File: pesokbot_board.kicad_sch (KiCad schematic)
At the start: 0 parts

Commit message: 01_Power_Input schem
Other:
- added sheet 01_Power_Input (01_Power_Input.kicad_sch)
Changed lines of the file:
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@@
 	(generator_version "10.0")
 	(paper "A4")
+	(sheet
+		(at 87.63 71.12)
+		(size 15.24 7.62)
+		(exclude_from_sim no)
+		(in_bom yes)
+		(on_board yes)
+		(dnp no)
+		(fields_autoplaced yes)
+		(stroke
+			(width 0.1524)
+			(type solid)
+		)
+		(fill
+			(color 0 0 0 0)
+		)
+		(property "Sheetname" "01_Power_Input"
+			(at 87.63 70.4084 0)
+			(show_name no)
+			(do_not_autoplace no)
+			(effects
+				(font
+					(size 1.27 1.27)
+				)
+				(justify left bottom)
+			)
+		)
+		(property "Sheetfile" "01_Power_Input.kicad_sch"
+			(at 87.63 79.3246 0)
+			(show_name no)
+			(do_not_autoplace no)
+			(effects
+				(font
+					(size 1.27 1.27)
+				)
+				(justify left top)
+			)
+		)
+		(instances
+			(project "pesokbot_board"
+				(path "/3b0b46ed-3ce3-4874-97d9-085fc63ec69d"
+					(page "2")
+				)
+			)
+		)
+	)
 	(sheet_instances
 		(path "/"

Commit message: 02_Servo_Power in progress
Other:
- added sheet 02_Servo_Power (Servo_Power.kicad_sch)
- sheet 01_Power_Input ports: added VBAT_PROT; removed none
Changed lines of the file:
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@@
 	(generator_version "10.0")
 	(paper "A4")
+	(wire
+		(pts
+			(xy 102.87 74.93) (xy 144.78 74.93)
+		)
+		(stroke
+			(width 0)
+			(type default)
+		)
+	)
+	(sheet
+		(at 137.16 71.12)
+		(size 16.51 7.62)
+		(exclude_from_sim no)
+		(in_bom yes)
+		(on_board yes)
+		(dnp no)
+		(fields_autoplaced yes)
+		(stroke
+			(width 0.1524)
+			(type solid)
+		)
+		(fill
+			(color 0 0 0 0)
+		)
+		(property "Sheetname" "02_Servo_Power"
+			(at 137.16 70.4084 0)
+			(show_name no)
+			(do_not_autoplace no)
+			(effects
+				(font
+					(size 1.27 1.27)
+				)
+				(justify left bottom)
+			)
+		)
+		(property "Sheetfile" "Servo_Power.kicad_sch"
+			(at 137.16 79.3246 0)
+			(show_name no)
+			(do_not_autoplace no)
+			(effects
+				(font
+					(size 1.27 1.27)
+				)
+				(justify left top)
+			)
+		)
+		(instances
+			(project "pesokbot_board"
+				(path "/3b0b46ed-3ce3-4874-97d9-085fc63ec69d"
+					(page "3")
+				)
+			)
+		)
+	)
 	(sheet
 		(at 87.63 71.12)
@@
 			)
 		)
+		(pin "VBAT_PROT" input
+			(at 102.87 74.93 0)
+			(effects
+				(font
+					(size 1.27 1.27)
+				)
+				(justify right)
+			)
+		)

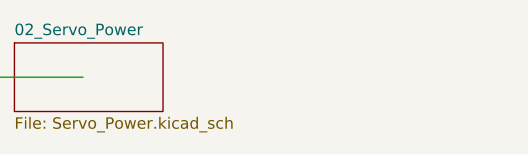
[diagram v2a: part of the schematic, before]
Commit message: BNO086 I2C connection added
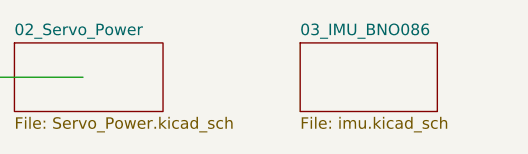
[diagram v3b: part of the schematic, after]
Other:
- added sheet 03_IMU_BNO086 (imu.kicad_sch)
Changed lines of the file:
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@@
+	)
+	(sheet
+		(at 168.91 71.12)
+		(size 15.24 7.62)
+		(exclude_from_sim no)
+		(in_bom yes)
+		(on_board yes)
+		(dnp no)
+		(fields_autoplaced yes)
+		(stroke
+			(width 0.1524)
+			(type solid)
+		)
+		(fill
+			(color 0 0 0 0)
+		)
+		(property "Sheetname" "03_IMU_BNO086"
+			(at 168.91 70.4084 0)
+			(show_name no)
+			(do_not_autoplace no)
+			(effects
+				(font
+					(size 1.27 1.27)
+				)
+				(justify left bottom)
+			)
+		)
+		(property "Sheetfile" "imu.kicad_sch"
+			(at 168.91 79.3246 0)
+			(show_name no)
+			(do_not_autoplace no)
+			(effects
+				(font
+					(size 1.27 1.27)
+				)
+				(justify left top)
+			)
+		)
+		(instances
+			(project "pesokbot_board"
+				(path "/3b0b46ed-3ce3-4874-97d9-085fc63ec69d"
+					(page "4")
+				)
+			)
+		)
 	)
 	(sheet

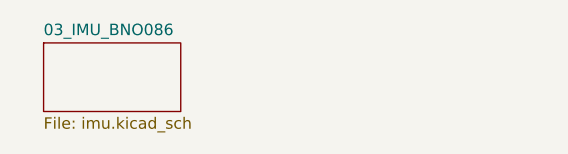
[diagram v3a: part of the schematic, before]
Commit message: add STM32H743ZIT6 schem
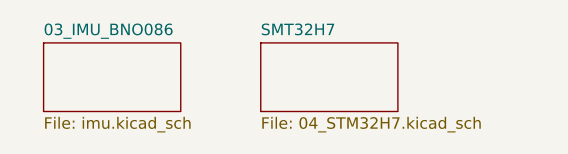
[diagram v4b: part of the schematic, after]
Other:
- added sheet SMT32H7 (04_STM32H7.kicad_sch)
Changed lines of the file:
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@@
+		)
+	)
+	(sheet
+		(at 193.04 71.12)
+		(size 15.24 7.62)
+		(exclude_from_sim no)
+		(in_bom yes)
+		(on_board yes)
+		(dnp no)
+		(fields_autoplaced yes)
+		(stroke
+			(width 0.1524)
+			(type solid)
+		)
+		(fill
+			(color 0 0 0 0)
+		)
+		(property "Sheetname" "SMT32H7"
+			(at 193.04 70.4084 0)
+			(show_name no)
+			(do_not_autoplace no)
+			(effects
+				(font
+					(size 1.27 1.27)
+				)
+				(justify left bottom)
+			)
+		)
+		(property "Sheetfile" "04_STM32H7.kicad_sch"
+			(at 193.04 79.3246 0)
+			(show_name no)
+			(do_not_autoplace no)
+			(effects
+				(font
+					(size 1.27 1.27)
+				)
+				(justify left top)
+			)
+		)
+		(instances
+			(project "pesokbot_board"
+				(path "/3b0b46ed-3ce3-4874-97d9-085fc63ec69d"
+					(page "5")
+				)
+			)
 		)
 	)

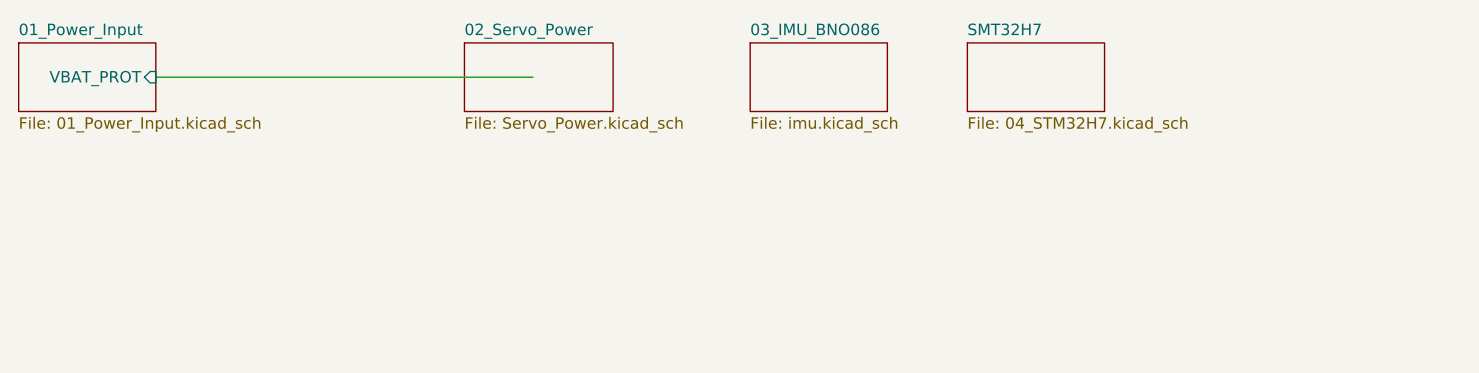
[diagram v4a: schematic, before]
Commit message: added USB-C CDC schem
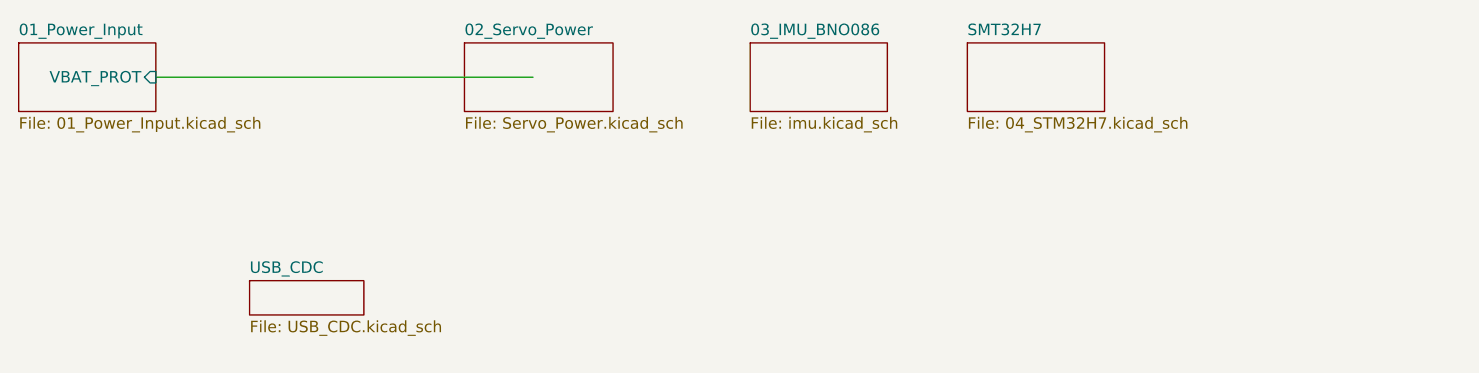
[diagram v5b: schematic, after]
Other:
- added sheet USB_CDC (USB_CDC.kicad_sch)
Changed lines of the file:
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@@
+	)
+	(sheet
+		(at 113.284 97.536)
+		(size 12.7 3.81)
+		(exclude_from_sim no)
+		(in_bom yes)
+		(on_board yes)
+		(dnp no)
+		(fields_autoplaced yes)
+		(stroke
+			(width 0.1524)
+			(type solid)
+		)
+		(fill
+			(color 0 0 0 0)
+		)
+		(property "Sheetname" "USB_CDC"
+			(at 113.284 96.8244 0)
+			(show_name no)
+			(do_not_autoplace no)
+			(effects
+				(font
+					(size 1.27 1.27)
+				)
+				(justify left bottom)
+			)
+		)
+		(property "Sheetfile" "USB_CDC.kicad_sch"
+			(at 113.284 101.9306 0)
+			(show_name no)
+			(do_not_autoplace no)
+			(effects
+				(font
+					(size 1.27 1.27)
+				)
+				(justify left top)
+			)
+		)
+		(instances
+			(project "pesokbot_board"
+				(path "/3b0b46ed-3ce3-4874-97d9-085fc63ec69d"
+					(page "6")
+				)
+			)
+		)
 	)
 	(sheet

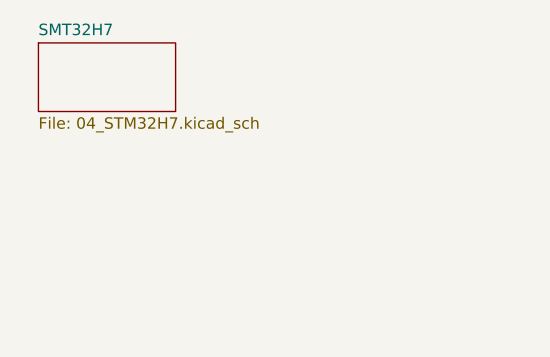
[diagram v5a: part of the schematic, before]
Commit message: added usb mcu and footprints
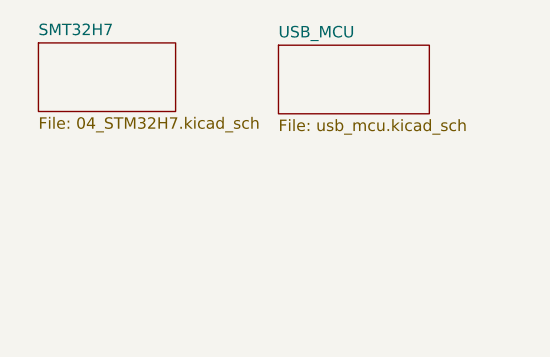
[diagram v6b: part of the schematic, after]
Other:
- added sheet USB_MCU (usb_mcu.kicad_sch)
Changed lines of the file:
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@@
+	)
+	(sheet
+		(at 219.71 71.374)
+		(size 16.764 7.62)
+		(exclude_from_sim no)
+		(in_bom yes)
+		(on_board yes)
+		(dnp no)
+		(fields_autoplaced yes)
+		(stroke
+			(width 0.1524)
+			(type solid)
+		)
+		(fill
+			(color 0 0 0 0)
+		)
+		(property "Sheetname" "USB_MCU"
+			(at 219.71 70.6624 0)
+			(show_name no)
+			(do_not_autoplace no)
+			(effects
+				(font
+					(size 1.27 1.27)
+				)
+				(justify left bottom)
+			)
+		)
+		(property "Sheetfile" "usb_mcu.kicad_sch"
+			(at 219.71 79.5786 0)
+			(show_name no)
+			(do_not_autoplace no)
+			(effects
+				(font
+					(size 1.27 1.27)
+				)
+				(justify left top)
+			)
+		)
+		(instances
+			(project "pesokbot_board"
+				(path "/3b0b46ed-3ce3-4874-97d9-085fc63ec69d"
+					(page "7")
+				)
+			)
+		)
 	)
 	(sheet

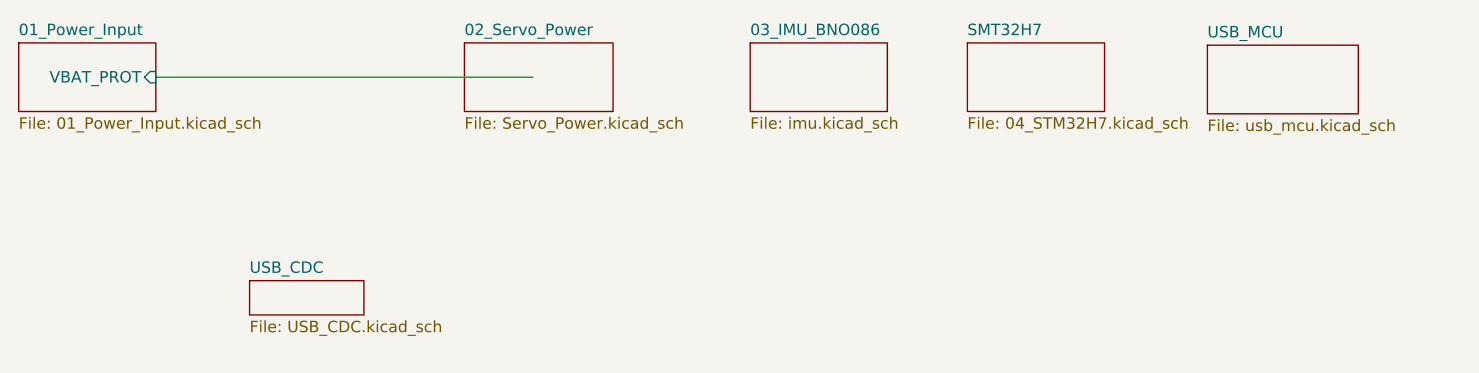
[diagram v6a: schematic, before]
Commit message: added user ports
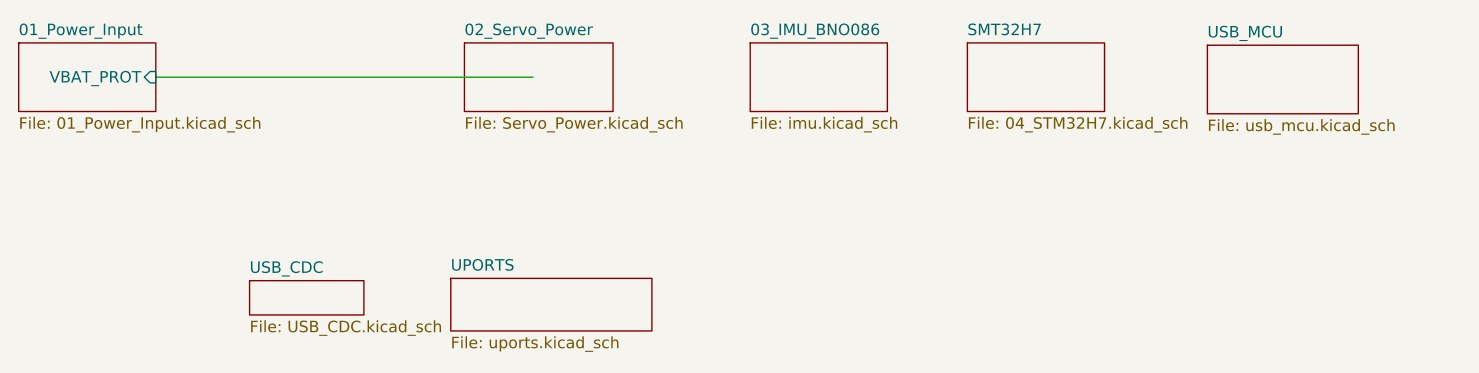
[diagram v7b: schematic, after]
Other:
- added sheet UPORTS (uports.kicad_sch)
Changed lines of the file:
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@@
+	)
+	(sheet
+		(at 135.636 97.282)
+		(size 22.352 5.842)
+		(exclude_from_sim no)
+		(in_bom yes)
+		(on_board yes)
+		(dnp no)
+		(fields_autoplaced yes)
+		(stroke
+			(width 0.1524)
+			(type solid)
+		)
+		(fill
+			(color 0 0 0 0)
+		)
+		(property "Sheetname" "UPORTS"
+			(at 135.636 96.5704 0)
+			(show_name no)
+			(do_not_autoplace no)
+			(effects
+				(font
+					(size 1.27 1.27)
+				)
+				(justify left bottom)
+			)
+		)
+		(property "Sheetfile" "uports.kicad_sch"
+			(at 135.636 103.7086 0)
+			(show_name no)
+			(do_not_autoplace no)
+			(effects
+				(font
+					(size 1.27 1.27)
+				)
+				(justify left top)
+			)
+		)
+		(instances
+			(project "pesokbot_board"
+				(path "/3b0b46ed-3ce3-4874-97d9-085fc63ec69d"
+					(page "8")
+				)
+			)
+		)
 	)
 	(sheet

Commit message: added 5v buck converter and place JST PH connectors
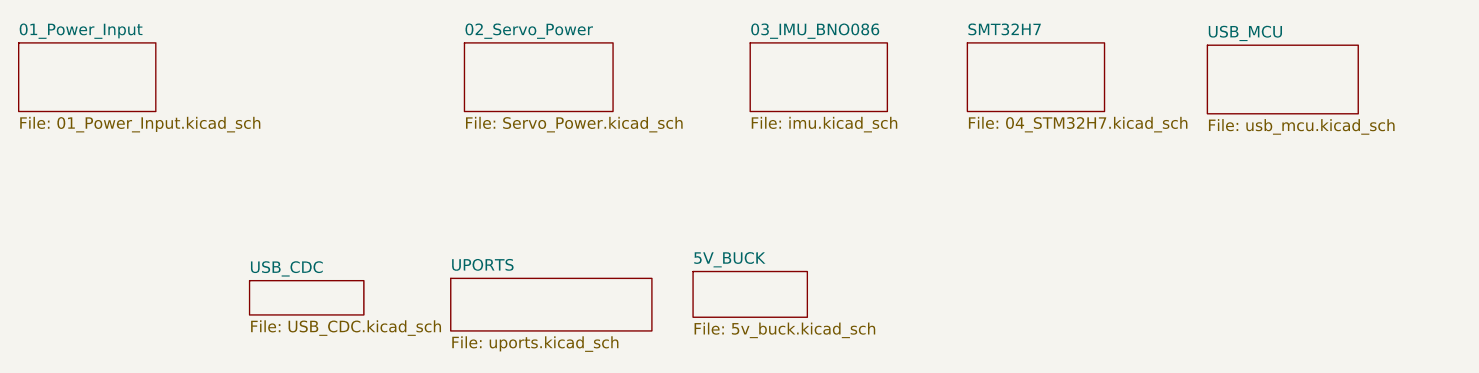
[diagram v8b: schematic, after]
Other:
- added sheet 5V_BUCK (5v_buck.kicad_sch)
- sheet 01_Power_Input ports: added none; removed VBAT_PROT
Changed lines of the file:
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@@
 	(generator_version "10.0")
 	(paper "A4")
-	(wire
-		(pts
-			(xy 102.87 74.93) (xy 144.78 74.93)
-		)
-		(stroke
-			(width 0)
-			(type default)
-		)
-	)
 	(sheet
 		(at 219.71 71.374)
@@
 			)
 		)
-		(pin "VBAT_PROT" input
-			(at 102.87 74.93 0)
-			(effects
-				(font
-					(size 1.27 1.27)
-				)
-				(justify right)
-			)
-		)
 		(instances
 			(project "pesokbot_board"
@@
 				)
 			)
+		)
+	)
+	(sheet
+		(at 162.56 96.52)
+		(size 12.7 5.08)
+		(exclude_from_sim no)
+		(in_bom yes)
+		(on_board yes)
+		(dnp no)
+		(fields_autoplaced yes)
+		(stroke
+			(width 0.1524)
+			(type solid)
+		)
+		(fill
+			(color 0 0 0 0)
+		)
+		(property "Sheetname" "5V_BUCK"
+			(at 162.56 95.8084 0)
+			(show_name no)
+			(do_not_autoplace no)
+			(effects
+				(font
+					(size 1.27 1.27)
+				)
+				(justify left bottom)
+			)
+		)
+		(property "Sheetfile" "5v_buck.kicad_sch"
+			(at 162.56 102.1846 0)
+			(show_name no)
+			(do_not_autoplace no)
+			(effects
+				(font
+					(size 1.27 1.27)
+				)
+				(justify left top)
+			)
+		)
+		(instances
+			(project "pesokbot_board"
+				(path "/3b0b46ed-3ce3-4874-97d9-085fc63ec69d"
+					(page "9")
+				)
+			)
